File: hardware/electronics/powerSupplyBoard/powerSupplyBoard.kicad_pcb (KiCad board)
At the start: 4 copper layers, 100 x 50 mm, 118 parts, among them J1 USB_C_Receptacle_USB2.0, J10 PREC002SAAN-RC, J11 S2B-PH-SM4-TB, J2 XT60PW-M, J3 S3B-XH-SM4-TB, J4 1729018, J5 Barrel_Jack_Switch, J6 PRPC009SBAN-M71RC, J8 PREC002SAAN-RC, J9 PREC003SAAN-RC, Q1 BUK961R6, Q2 CSD18532Q5B, Q3 CSD18532Q5B, Q4 BSS84, Q5 2N7002, Q6 2N7002, SW1 PTS647, SW2 SS-12D07, U1 STM32L052K6, U2 AP2112K-3.3, U3 SN65HVD230QDR, U4 BQ25798, U5 BQ76905, U6 BQ34Z100-R2, Y1 ECS-327ATQMV

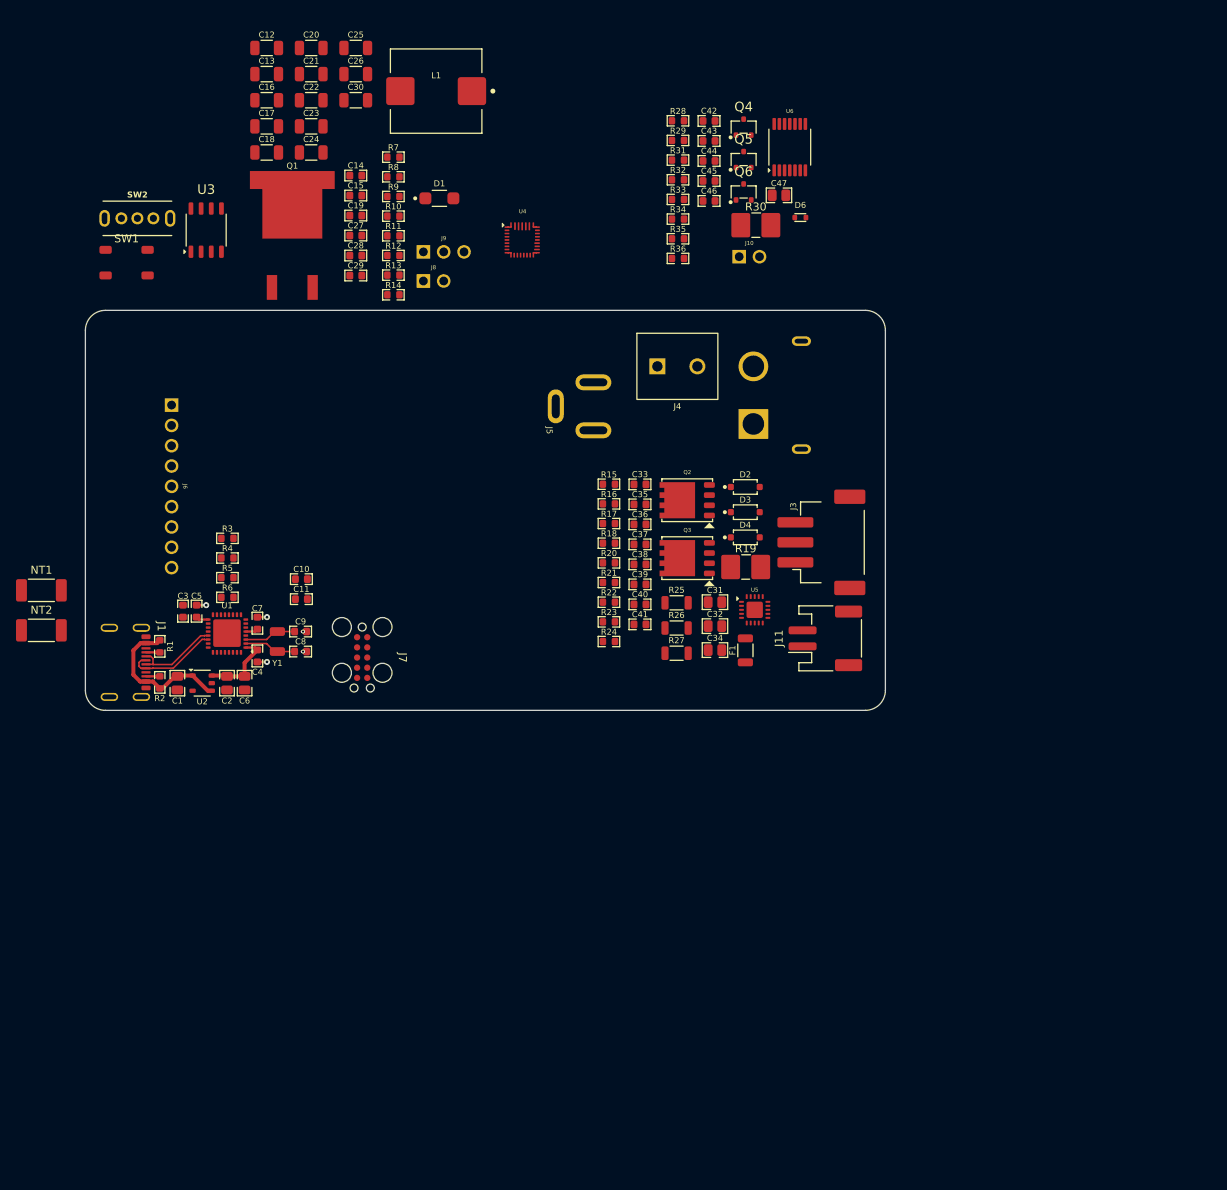
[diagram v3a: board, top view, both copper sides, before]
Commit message: updated sch merge. started routing controller stuff
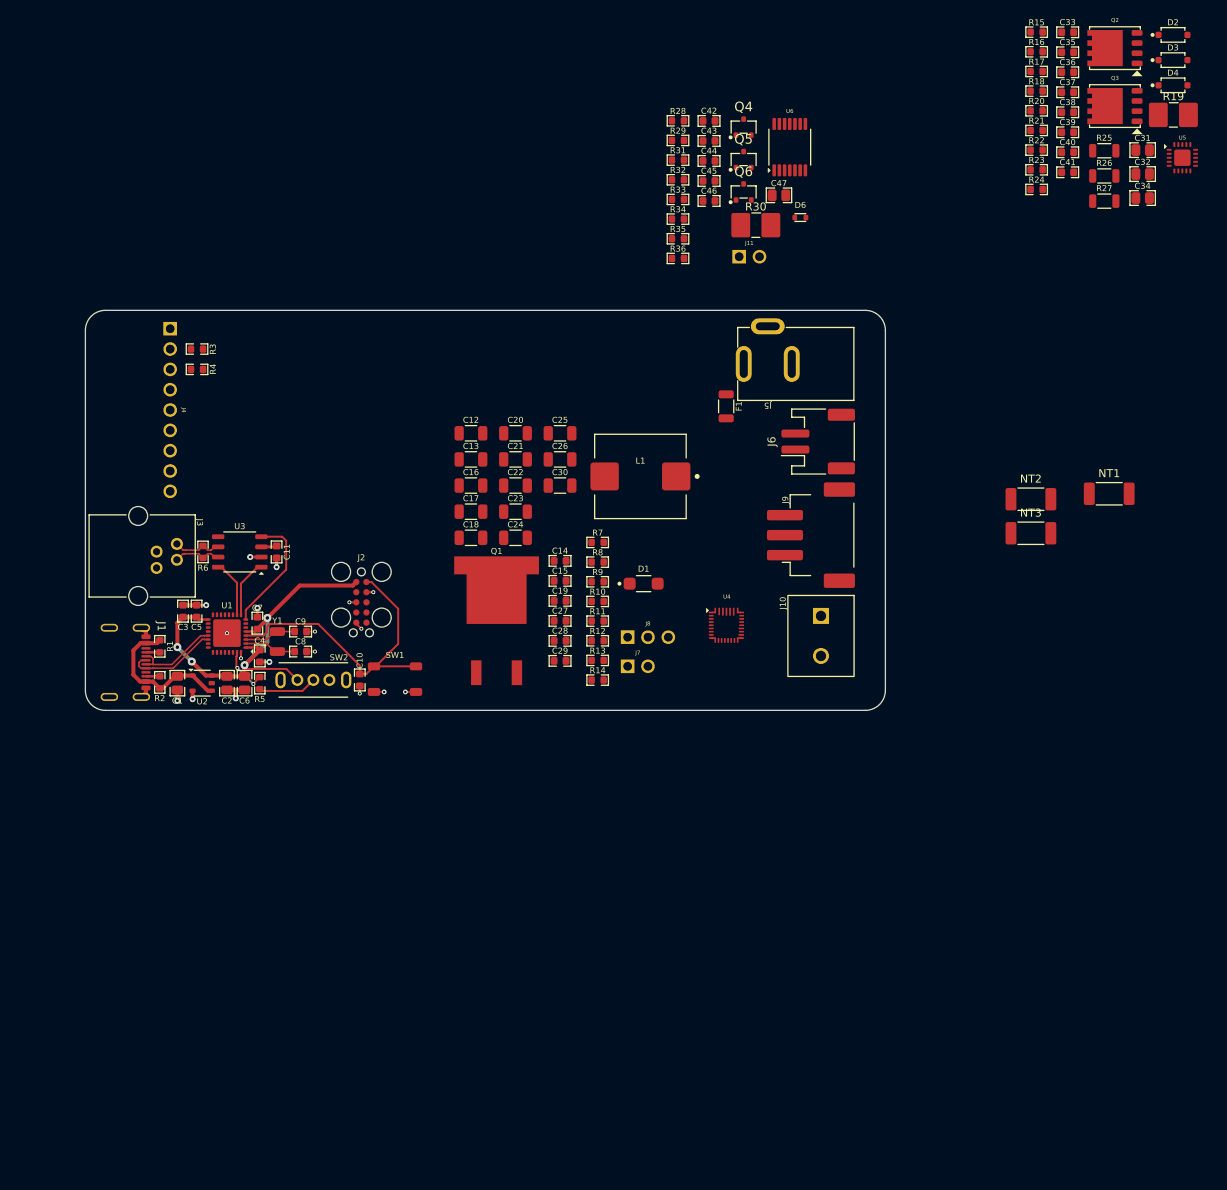
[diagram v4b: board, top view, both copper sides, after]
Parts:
- removed the J2 at (174.5, 60.6)
- removed the J4 at (159.0, 57.0)
- added J10: 1729018, DS-Rectangular-Connectors:5mmTerminalBlock, F.Cu at (176.9, 90.7)
- added J9: S3B-XH-SM4-TB, DS-Rectangular-Connectors:JST_XH_S3B-SM4-TB, F.Cu at (175.7, 78.1)
- added NT3: Net-Tie, DS-Resistors-SMD:CRCW1210, F.Cu at (203.2, 77.9)
- J3: value S3B-XH-SM4-TB -> 615004143821; footprint DS-Rectangular-Connectors:JST_XH_S3B-SM4-TB -> DS-Connectors-Network:615004143821
- moved NT1 134.0 mm to (213.0, 72.9)
- moved NT2 124.8 mm to (203.2, 73.6)
- moved J3 85.4 mm to (91.6, 80.7), turned to -90 degrees
- moved Q3 77.8 mm to (213.7, 24.5)
- moved R15 77.8 mm to (203.9, 15.2)
- moved R16 77.8 mm to (203.9, 17.7)
- moved R17 77.8 mm to (203.9, 20.1)
- moved R24 77.8 mm to (203.9, 34.9)
- moved C33 77.8 mm to (207.8, 15.2)
- moved C35 77.8 mm to (207.8, 17.7)
- moved C36 77.8 mm to (207.8, 20.2)
- moved C37 77.8 mm to (207.8, 22.7)
- moved C38 77.8 mm to (207.8, 25.2)
- moved C39 77.8 mm to (207.8, 27.7)
- moved C40 77.8 mm to (207.8, 30.2)
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- renumbered J10 to J11, J7 to J2, J6 to J4, J11 to J6, J8 to J7, J9 to J8
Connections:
- net VIN renamed Net-(F1-Pad1)
- C1 pad 2: GND -> VSS
- C10 pad 2: GND -> VSS
- C11 pad 2: GND -> VSS
- C2 pad 2: GND -> VSS
- C3 pad 2: GND -> VSS
- C37 pad 1: Net-(C37-Pad1) -> SENSE-
- C38 pad 2: /PACK- -> VSS
- C4 pad 2: GND -> VSS
- C5 pad 2: GND -> VSS
- C6 pad 2: GND -> VSS
- C7 pad 2: GND -> VSS
- C8 pad 2: GND -> VSS
- C9 pad 2: GND -> VSS
- D4 pad 1: /PACK- -> VSS
- J1 pad A1: GND -> VSS
- J1 pad A12: GND -> VSS
- J1 pad B1: GND -> VSS
- J1 pad B12: GND -> VSS
- J1 pad S1: GND -> VSS
- J2 pad 3: GND -> VSS
- J2 pad 5: GND -> VSS
- J2 pad 9: GND -> VSS
- J3 pad 1: BAT+ -> unconnected-(J3-Pad1)
- J3 pad 2: /1P -> /CAN_P
- J3 pad 3: /BAT- -> /CAN_N
- J4 pad 1: /VBUS -> /VUSB
- J4 pad 9: GND -> VSS
- J6 pad 2: GND -> AGND
- J6 pad MP: Net-(J11-PadMP) -> unconnected-(J6-PadMP)
- J7 pad 2: GND -> AGND
- J8 pad 3: GND -> AGND
- NT1 pad 1: /BAT- -> GND
- NT1 pad 2: GND -> AGND
- NT2 pad 1: /BAT- -> /Battery Monitor/1P
- NT2 pad 2: AGND -> GND
- Q2 pad 1: Net-(C37-Pad1) -> SENSE-
- Q2 pad 2: Net-(C37-Pad1) -> SENSE-
- Q2 pad 3: Net-(C37-Pad1) -> SENSE-
- Q3 pad 1: /PACK- -> VSS
- Q3 pad 2: /PACK- -> VSS
- Q3 pad 3: /PACK- -> VSS
- R12 pad 2: GND -> AGND
- R14 pad 2: GND -> AGND
- R17 pad 2: /BAT- -> SENSE+
- R18 pad 2: Net-(C37-Pad1) -> SENSE-
- R19 pad 1: /BAT- -> SENSE+
- R19 pad 2: Net-(C37-Pad1) -> SENSE-
- R20 pad 2: Net-(C37-Pad1) -> SENSE-
- R23 pad 2: /PACK- -> VSS
- R26 pad 1: /1P -> /Battery Monitor/1P
- R27 pad 1: /BAT- -> GND
- R28 pad 2: /PACK- -> SENSE-
- R29 pad 2: /BAT- -> SENSE+
- R30 pad 1: /PACK- -> SENSE-
- R30 pad 2: /BAT- -> SENSE+
- R6 pad 1: Net-(U3-CANH) -> /CAN_P
- R6 pad 2: Net-(U3-CANL) -> /CAN_N
- R9 pad 2: GND -> AGND
- SW1 pad 2: GND -> /NRST
- SW1 pad 3: GND -> VSS
- SW1 pad 4: /NRST -> VSS
- SW2 pad 3: GND -> VSS
- U1 pad 10: unconnected-(U1-PA4-Pad10) -> /CAN_MODE
- U1 pad 16: GND -> VSS
- U1 pad 18: /CAN_MODE -> unconnected-(U1-PA8-Pad18)
- U1 pad 19: /CAN_TXD -> unconnected-(U1-PA9-Pad19)
- U1 pad 20: /CAN_RXD -> unconnected-(U1-PA10-Pad20)
- U1 pad 32: GND -> VSS
- U1 pad 33: GND -> VSS
- U1 pad 8: unconnected-(U1-PA2-Pad8) -> /CAN_TXD
- U1 pad 9: unconnected-(U1-PA3-Pad9) -> /CAN_RXD
- U2 pad 2: GND -> VSS
- U3 pad 2: GND -> VSS
- U3 pad 6: Net-(U3-CANL) -> /CAN_N
- U3 pad 7: Net-(U3-CANH) -> /CAN_P
- U4 pad 10: GND -> AGND
- U4 pad 11: GND -> AGND
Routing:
- net +3V3: track 12.8 -> 55.9 mm, vias 0 -> 4
- net /NRST: track 0.00 -> 39.8 mm
- net VSS: track 0.00 -> 25.3 mm, vias 0 -> 11
- net /CAN_TXD: track 0.00 -> 15.3 mm
- net Net-(R5-Pad2): track 0.00 -> 7.36 mm
- net /CAN_RXD: track 0.00 -> 7.30 mm
- net /CAN_MODE: track 0.00 -> 7.16 mm
- net /CAN_N: track 0.00 -> 6.09 mm
- net /CAN_P: track 0.00 -> 6.09 mm
- net Net-(U1-BOOT0): track 0.00 -> 6.05 mm, vias 0 -> 2
- net GND: track 5.70 -> 0.00 mm, vias 5 -> 7
- added copper zone on In1.Cu, net VSS
- added copper zone on In2.Cu, net VSS
- removed copper zone on In1.Cu, net GND
- removed copper zone on In2.Cu, net GND
